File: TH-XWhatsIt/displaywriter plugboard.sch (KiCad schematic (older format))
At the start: 4 parts, among them J10 DISPLAYWRITER PLUGBOARD CONNE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, J11 DISPLAYWRITER PLUGBOARD ROWS, J9 DISPLAYWRITER PLUGBOARD COLUM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

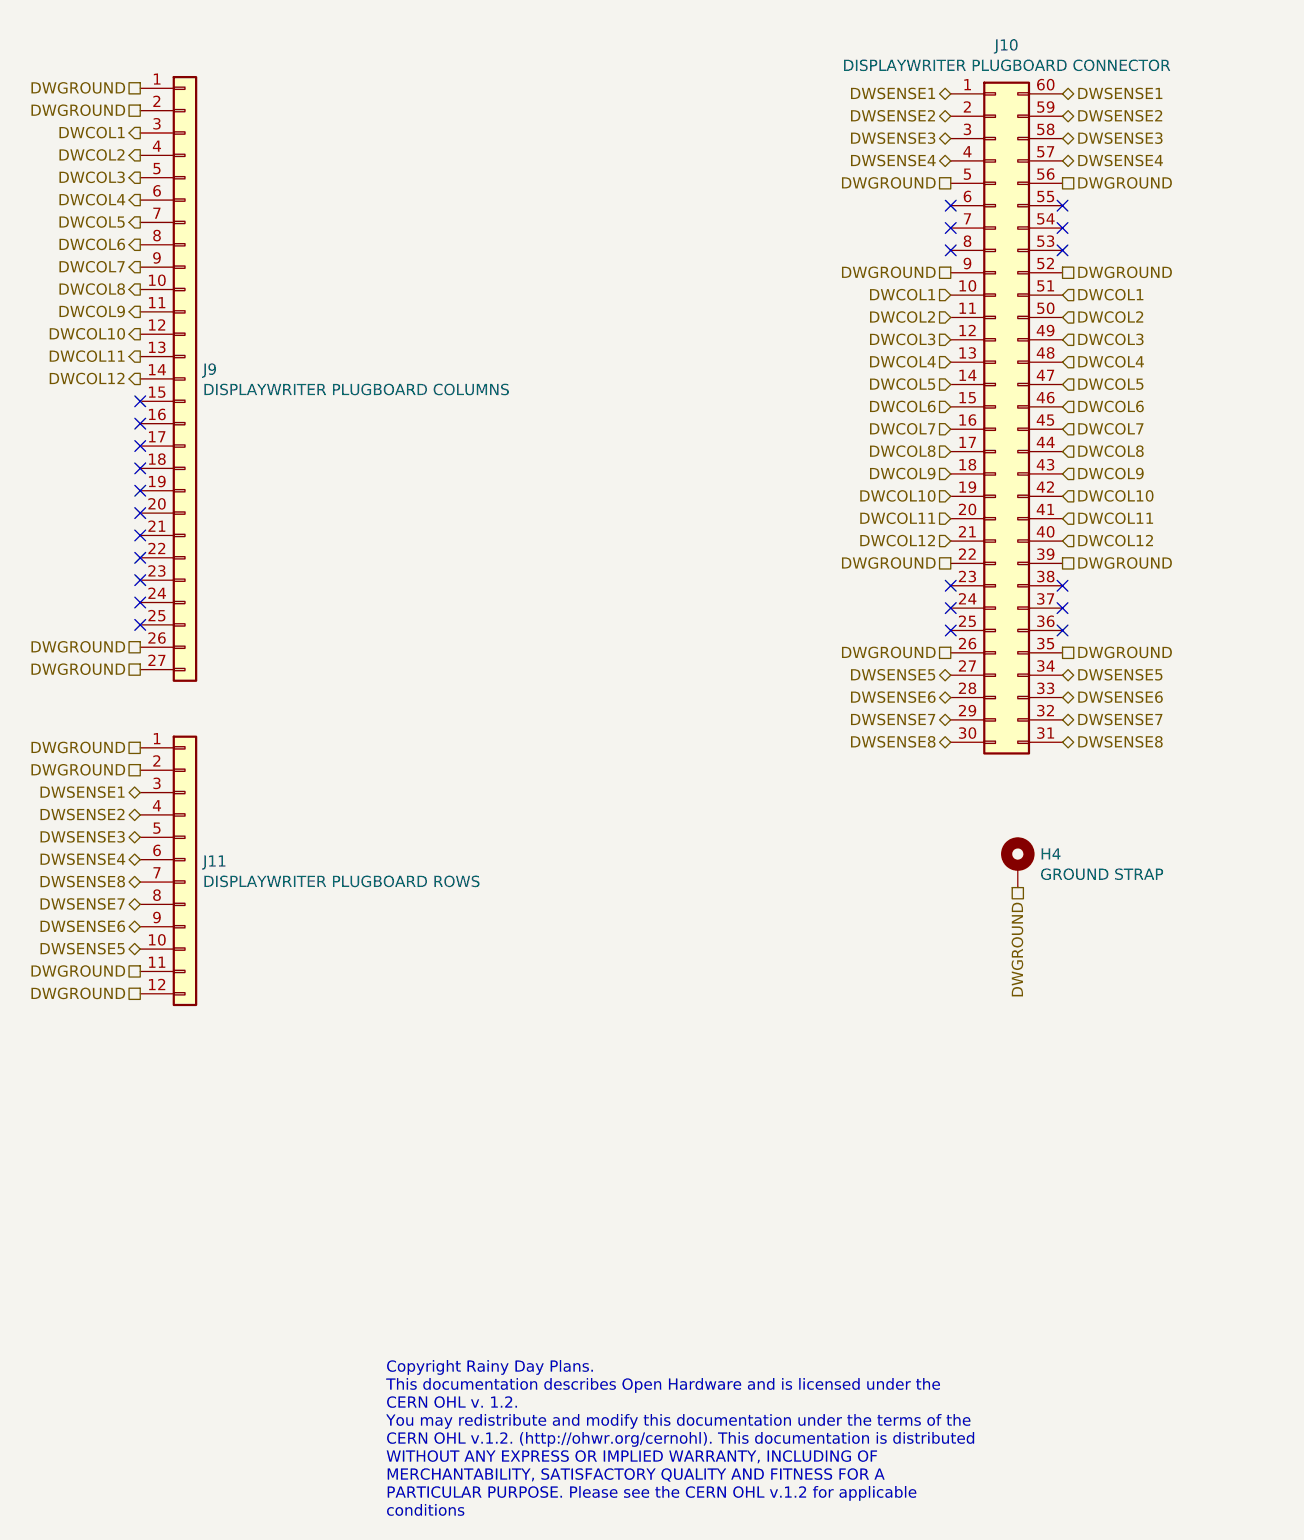
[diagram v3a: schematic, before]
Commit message: initial update to switch to smd, so now th prefix is a misnomer
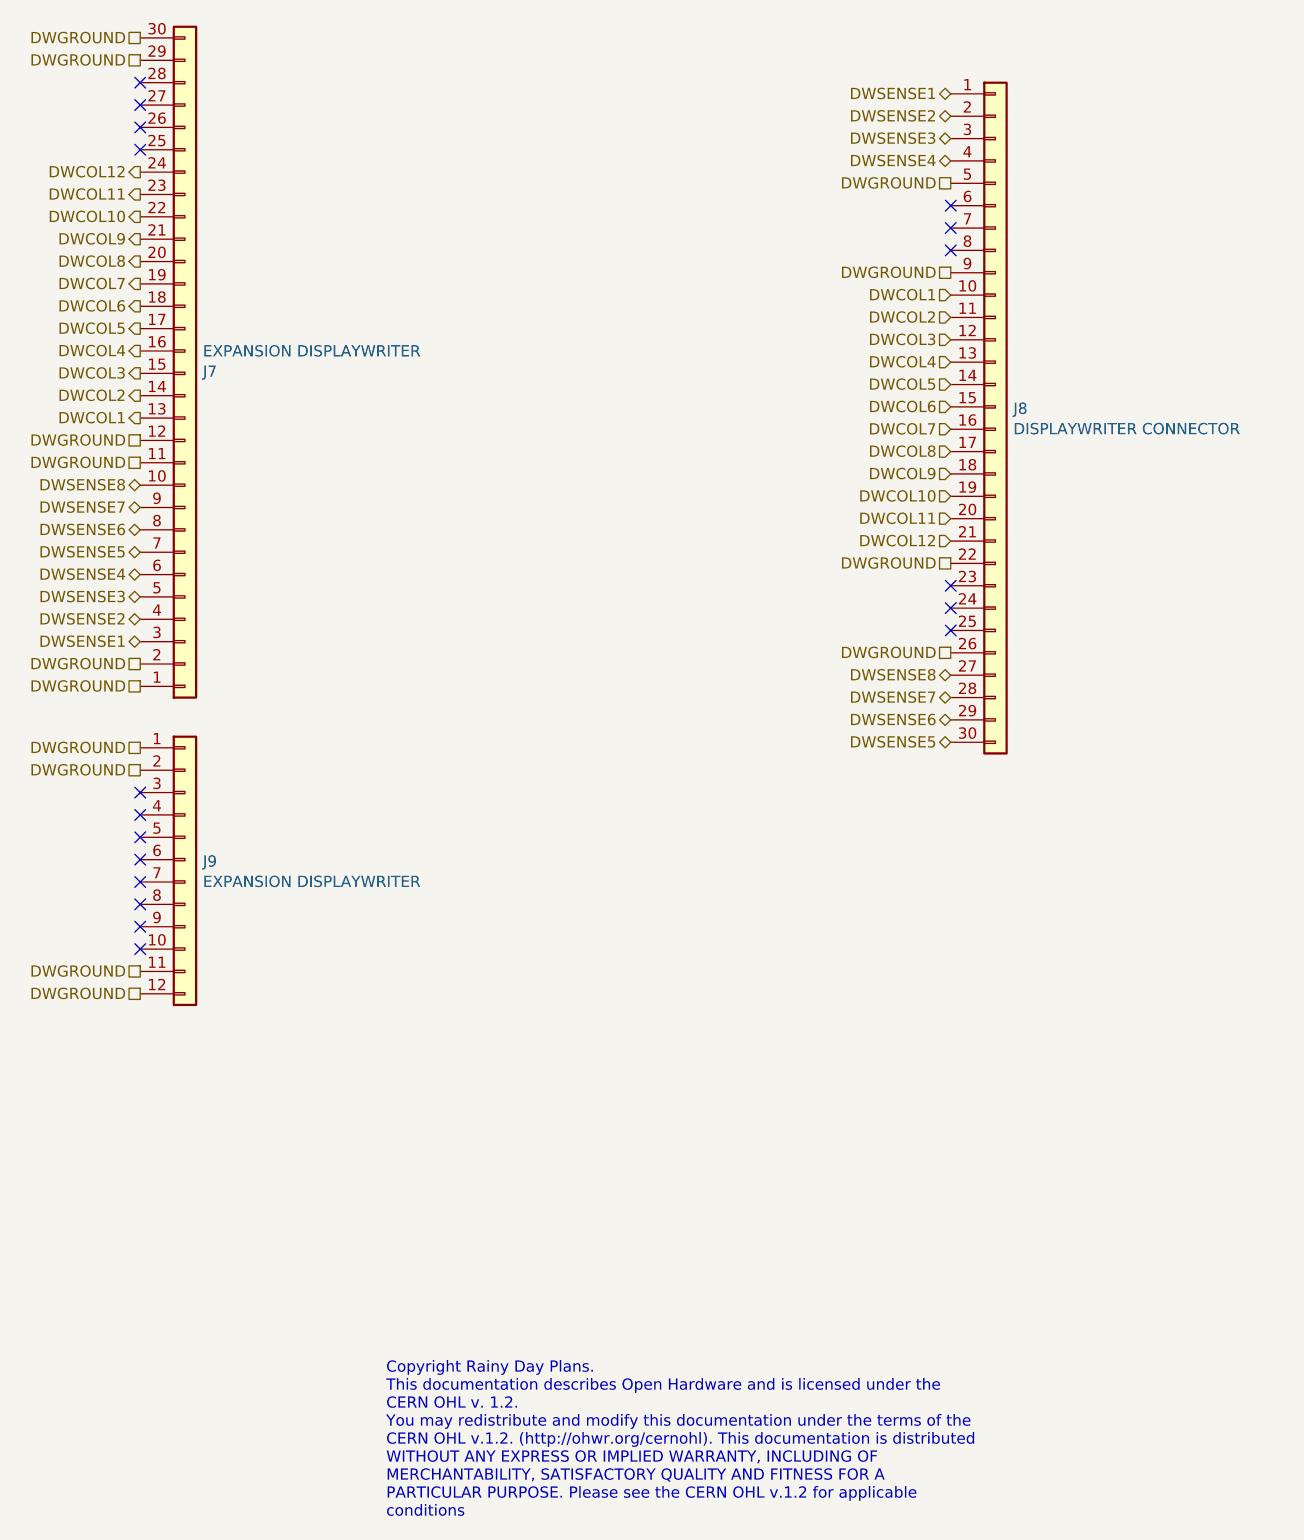
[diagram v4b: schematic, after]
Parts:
- removed H4: GROUND STRAP, MountingHole:MountingHole_2.2mm_M2_Pad_Via, symbol Mechanical:MountingHole_Pad
- removed J10: DISPLAYWRITER PLUGBOARD CONNECTOR, TH-XWhatsIt:DIP-60_155_ELL, symbol Connector_Generic:Conn_02x30_Counter_Clockwise
- removed J9: DISPLAYWRITER PLUGBOARD COLUMNS, Connector_PinSocket_2.54mm:PinSocket_1x27_P2.54mm_Vertical, symbol Connector_Generic:Conn_01x27
- added J7: EXPANSION DISPLAYWRITER, TH-XWhatsIt:30-pin-castelated-connector, symbol Connector_Generic:Conn_01x30
- added J8: DISPLAYWRITER CONNECTOR, TH-XWhatsIt:30-pin-universal-beamspring-connector, symbol Connector_Generic:Conn_01x30
- J9: renamed from J11; value DISPLAYWRITER PLUGBOARD ROWS -> EXPANSION DISPLAYWRITER; footprint Connector_PinSocket_2.54mm:PinSocket_1x12_P2.54mm_Vertical -> TH-XWhatsIt:12-pin-castelated-connector
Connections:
- net DWCOL1: now also J7.13 (Pin_13), J8.10 (Pin_10)
- net DWCOL10: now also J7.22 (Pin_22), J8.19 (Pin_19)
- net DWCOL11: now also J7.23 (Pin_23), J8.20 (Pin_20)
- net DWCOL12: now also J7.24 (Pin_24), J8.21 (Pin_21)
- net DWCOL2: now also J7.14 (Pin_14), J8.11 (Pin_11)
- net DWCOL3: now also J7.15 (Pin_15), J8.12 (Pin_12)
- net DWCOL4: now also J7.16 (Pin_16), J8.13 (Pin_13)
- net DWCOL5: now also J7.17 (Pin_17), J8.14 (Pin_14)
- net DWCOL6: now also J7.18 (Pin_18), J8.15 (Pin_15)
- net DWCOL7: now also J7.19 (Pin_19), J8.16 (Pin_16)
- net DWCOL8: now also J7.20 (Pin_20), J8.17 (Pin_17)
- net DWCOL9: now also J7.21 (Pin_21), J8.18 (Pin_18)
- net DWGROUND: now also J7.1 (Pin_1), J7.11 (Pin_11), J7.12 (Pin_12), J7.2 (Pin_2), J7.29 (Pin_29), J7.30 (Pin_30), J8.22 (Pin_22), J8.26 (Pin_26), J8.5 (Pin_5), J8.9 (Pin_9)
- net DWSENSE1: now also J7.3 (Pin_3), J8.1 (Pin_1); no longer J9.3 (Pin_3)
- net DWSENSE2: now also J7.4 (Pin_4), J8.2 (Pin_2); no longer J9.4 (Pin_4)
- net DWSENSE3: now also J7.5 (Pin_5), J8.3 (Pin_3); no longer J9.5 (Pin_5)
- net DWSENSE4: now also J7.6 (Pin_6), J8.4 (Pin_4); no longer J9.6 (Pin_6)
- net DWSENSE5: now also J7.7 (Pin_7), J8.30 (Pin_30); no longer J9.10 (Pin_10)
- net DWSENSE6: now also J7.8 (Pin_8), J8.29 (Pin_29); no longer J9.9 (Pin_9)
- net DWSENSE7: now also J7.9 (Pin_9), J8.28 (Pin_28); no longer J9.8 (Pin_8)
- net DWSENSE8: now also J7.10 (Pin_10), J8.27 (Pin_27); no longer J9.7 (Pin_7)
- no-connect marks 23 -> 18
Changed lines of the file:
@@
 $Descr A4 11693 8268
 encoding utf-8
-Sheet 4 4
+Sheet 3 3
 Title "Displaywriter plugboard to convert controller signals"
 Date "2020-01-31"
@@
 $EndDescr
 $Comp
-L Connector_Generic:Conn_01x27 J?
-U 1 1 5E97F100
-P 3050 2650
-AR Path="/5E97F100" Ref="J?"  Part="1"
-AR Path="/5E97697F/5E97F100" Ref="J?"  Part="1"
-AR Path="/5E995B14/5E97F100" Ref="J9"  Part="1"
-F 0 "J9" H 3130 2692 50  0000 L CNN
-F 1 "DISPLAYWRITER PLUGBOARD COLUMNS" H 3130 2601 50  0000 L CNN
-F 2 "Connector_PinSocket_2.54mm:PinSocket_1x27_P2.54mm_Vertical" H 3050 2650 50  0001 C CNN
-F 3 "~" H 3050 2650 50  0001 C CNN
-	1    3050 2650
-	1    0    0    -1
-$EndComp
-$Comp
 L Connector_Generic:Conn_01x12 J?
 U 1 1 5E97F11D
@@
 AR Path="/5E97F11D" Ref="J?"  Part="1"
 AR Path="/5E97697F/5E97F11D" Ref="J?"  Part="1"
-AR Path="/5E995B14/5E97F11D" Ref="J11"  Part="1"
-F 0 "J11" H 3130 4792 50  0000 L CNN
-F 1 "DISPLAYWRITER PLUGBOARD ROWS" H 3130 4701 50  0000 L CNN
-F 2 "Connector_PinSocket_2.54mm:PinSocket_1x12_P2.54mm_Vertical" H 3050 4800 50  0001 C CNN
+AR Path="/5E995B14/5E97F11D" Ref="J9"  Part="1"
+F 0 "J9" H 3130 4792 50  0000 L CNN
+F 1 "EXPANSION DISPLAYWRITER" H 3130 4701 50  0000 L CNN
+F 2 "TH-XWhatsIt:12-pin-castelated-connector" H 3050 4800 50  0001 C CNN
 F 3 "~" H 3050 4800 50  0001 C CNN
 	1    3050 4800
@@
 NoConn ~ 6475 1975
 NoConn ~ 6475 2075
-Text HLabel 2850 1550 0    50   Output ~ 0
-DWCOL1
-Text HLabel 2850 1650 0    50   Output ~ 0
-DWCOL2
-Text HLabel 2850 1750 0    50   Output ~ 0
-DWCOL3
-Text HLabel 2850 1850 0    50   Output ~ 0
-DWCOL4
-Text HLabel 2850 1950 0    50   Output ~ 0
-DWCOL5
-Text HLabel 2850 2050 0    50   Output ~ 0
-DWCOL6
-Text HLabel 2850 2150 0    50   Output ~ 0
-DWCOL7
-Text HLabel 2850 2250 0    50   Output ~ 0
-DWCOL8
-Text HLabel 2850 2350 0    50   Output ~ 0
-DWCOL9
-Text HLabel 2850 2450 0    50   Output ~ 0
-DWCOL10
-Text HLabel 2850 2550 0    50   Output ~ 0
-DWCOL11
-Text HLabel 2850 2650 0    50   Output ~ 0
-DWCOL12
-Text HLabel 2850 4500 0    50   BiDi ~ 0
-DWSENSE1
-Text HLabel 2850 4600 0    50   BiDi ~ 0
-DWSENSE2
-Text HLabel 2850 4700 0    50   BiDi ~ 0
-DWSENSE3
-Text HLabel 2850 4800 0    50   BiDi ~ 0
-DWSENSE4
-Text HLabel 2850 5200 0    50   BiDi ~ 0
-DWSENSE5
-Text HLabel 2850 5100 0    50   BiDi ~ 0
-DWSENSE6
-Text HLabel 2850 5000 0    50   BiDi ~ 0
-DWSENSE7
-Text HLabel 2850 4900 0    50   BiDi ~ 0
-DWSENSE8
 Text HLabel 6475 1375 0    50   BiDi ~ 0
 DWSENSE1
@@
 Text HLabel 6475 1675 0    50   BiDi ~ 0
 DWSENSE4
+Text HLabel 6475 4275 0    50   BiDi ~ 0
+DWSENSE5
+Text HLabel 6475 4175 0    50   BiDi ~ 0
+DWSENSE6
+Text HLabel 6475 4075 0    50   BiDi ~ 0
+DWSENSE7
 Text HLabel 6475 3975 0    50   BiDi ~ 0
-DWSENSE5
-Text HLabel 6475 4075 0    50   BiDi ~ 0
-DWSENSE6
-Text HLabel 6475 4175 0    50   BiDi ~ 0
-DWSENSE7
-Text HLabel 6475 4275 0    50   BiDi ~ 0
 DWSENSE8
 Text HLabel 6475 2275 0    50   Input ~ 0
@@
 Text HLabel 6475 3375 0    50   Input ~ 0
 DWCOL12
-Text HLabel 2850 1350 0    50   UnSpc ~ 0
+Text HLabel 2850 1125 0    50   UnSpc ~ 0
 DWGROUND
-Text HLabel 2850 1450 0    50   UnSpc ~ 0
+Text HLabel 2850 1225 0    50   UnSpc ~ 0
 DWGROUND
-Text HLabel 2850 3850 0    50   UnSpc ~ 0
+Text HLabel 2850 3925 0    50   UnSpc ~ 0
 DWGROUND
-Text HLabel 2850 3950 0    50   UnSpc ~ 0
+Text HLabel 2850 4025 0    50   UnSpc ~ 0
 DWGROUND
 Text HLabel 2850 4300 0    50   UnSpc ~ 0
@@
 Text HLabel 6475 3875 0    50   UnSpc ~ 0
 DWGROUND
-NoConn ~ 2850 2750
-NoConn ~ 2850 2850
-NoConn ~ 2850 2950
-NoConn ~ 2850 3050
-NoConn ~ 2850 3150
-NoConn ~ 2850 3250
-NoConn ~ 2850 3350
-NoConn ~ 2850 3450
-NoConn ~ 2850 3550
-NoConn ~ 2850 3650
-NoConn ~ 2850 3750
 Text Notes 3950 7750 0    50   ~ 0
 Copyright Rainy Day Plans.\nThis documentation describes Open Hardware and is licensed under the\nCERN OHL v. 1.2.\nYou may redistribute and modify this documentation under the terms of the\nCERN OHL v.1.2. (http://ohwr.org/cernohl). This documentation is distributed\nWITHOUT ANY EXPRESS OR IMPLIED WARRANTY, INCLUDING OF\nMERCHANTABILITY, SATISFACTORY QUALITY AND FITNESS FOR A\nPARTICULAR PURPOSE. Please see the CERN OHL v.1.2 for applicable\nconditions
+Text HLabel 2850 3825 0    50   BiDi ~ 0
+DWSENSE1
+Text HLabel 2850 3725 0    50   BiDi ~ 0
+DWSENSE2
+Text HLabel 2850 3625 0    50   BiDi ~ 0
+DWSENSE3
+Text HLabel 2850 3525 0    50   BiDi ~ 0
+DWSENSE4
+Text HLabel 2850 3425 0    50   BiDi ~ 0
+DWSENSE5
+Text HLabel 2850 3325 0    50   BiDi ~ 0
+DWSENSE6
+Text HLabel 2850 3225 0    50   BiDi ~ 0
+DWSENSE7
+Text HLabel 2850 3125 0    50   BiDi ~ 0
+DWSENSE8
+Text HLabel 2850 2925 0    50   UnSpc ~ 0
+DWGROUND
+Text HLabel 2850 3025 0    50   UnSpc ~ 0
+DWGROUND
 $Comp
-L Connector_Generic:Conn_02x30_Counter_Clockwise J10
-U 1 1 5E4284EA
+L Connector_Generic:Conn_01x30 J?
+U 1 1 5F5BFC0E
+P 3050 2625
+AR Path="/5F5BFC0E" Ref="J?"  Part="1"
+AR Path="/5E995B14/5F5BFC0E" Ref="J7"  Part="1"
+F 0 "J7" H 3130 2617 50  0000 L CNN
+F 1 "EXPANSION DISPLAYWRITER" H 3130 2526 50  0000 L CNN
+F 2 "TH-XWhatsIt:30-pin-castelated-connector" H 3050 2625 50  0001 C CNN
+F 3 "~" H 3050 2625 50  0001 C CNN
+	1    3050 2625
+	1    0    0    1
+$EndComp
+$Comp
+L Connector_Generic:Conn_01x30 J?
+U 1 1 5F5CA487
 P 6675 2775
-F 0 "J10" H 6725 4392 50  0000 C CNN
-F 1 "DISPLAYWRITER PLUGBOARD CONNECTOR" H 6725 4301 50  0000 C CNN
-F 2 "TH-XWhatsIt:DIP-60_155_ELL" H 6675 2775 50  0001 C CNN
+AR Path="/5F5CA487" Ref="J?"  Part="1"
+AR Path="/5E995B14/5F5CA487" Ref="J8"  Part="1"
+F 0 "J8" H 6755 2767 50  0000 L CNN
+F 1 "DISPLAYWRITER CONNECTOR" H 6755 2676 50  0000 L CNN
+F 2 "TH-XWhatsIt:30-pin-universal-beamspring-connector" H 6675 2775 50  0001 C CNN
 F 3 "~" H 6675 2775 50  0001 C CNN
 	1    6675 2775
 	1    0    0    -1
 $EndComp
-NoConn ~ 6975 3575
-NoConn ~ 6975 3675
-NoConn ~ 6975 3775
-NoConn ~ 6975 1875
-NoConn ~ 6975 1975
-NoConn ~ 6975 2075
-Text HLabel 6975 1375 2    50   BiDi ~ 0
-DWSENSE1
-Text HLabel 6975 1475 2    50   BiDi ~ 0
-DWSENSE2
-Text HLabel 6975 1575 2    50   BiDi ~ 0
-DWSENSE3
-Text HLabel 6975 1675 2    50   BiDi ~ 0
-DWSENSE4
-Text HLabel 6975 3975 2    50   BiDi ~ 0
-DWSENSE5
-Text HLabel 6975 4075 2    50   BiDi ~ 0
-DWSENSE6
-Text HLabel 6975 4175 2    50   BiDi ~ 0
-DWSENSE7
-Text HLabel 6975 4275 2    50   BiDi ~ 0
-DWSENSE8
-Text HLabel 6975 2275 2    50   Input ~ 0
+NoConn ~ 2850 4500
+NoConn ~ 2850 4600
+NoConn ~ 2850 4700
+NoConn ~ 2850 4800
+NoConn ~ 2850 4900
+NoConn ~ 2850 5000
+NoConn ~ 2850 5100
+NoConn ~ 2850 5200
+Text HLabel 2850 1725 0    50   Output ~ 0
+DWCOL12
+Text HLabel 2850 1825 0    50   Output ~ 0
+DWCOL11
+Text HLabel 2850 1925 0    50   Output ~ 0
+DWCOL10
+Text HLabel 2850 2025 0    50   Output ~ 0
+DWCOL9
+Text HLabel 2850 2125 0    50   Output ~ 0
+DWCOL8
+Text HLabel 2850 2225 0    50   Output ~ 0
+DWCOL7
+Text HLabel 2850 2325 0    50   Output ~ 0
+DWCOL6
+Text HLabel 2850 2425 0    50   Output ~ 0
+DWCOL5
+Text HLabel 2850 2525 0    50   Output ~ 0
+DWCOL4
+Text HLabel 2850 2625 0    50   Output ~ 0
+DWCOL3
+Text HLabel 2850 2725 0    50   Output ~ 0
+DWCOL2
+Text HLabel 2850 2825 0    50   Output ~ 0
 DWCOL1
-Text HLabel 6975 2375 2    50   Input ~ 0
-DWCOL2
-Text HLabel 6975 2475 2    50   Input ~ 0
-DWCOL3
-Text HLabel 6975 2575 2    50   Input ~ 0
-DWCOL4
-Text HLabel 6975 2675 2    50   Input ~ 0
-DWCOL5
-Text HLabel 6975 2775 2    50   Input ~ 0
-DWCOL6
-Text HLabel 6975 2875 2    50   Input ~ 0
-DWCOL7
-Text HLabel 6975 2975 2    50   Input ~ 0
-DWCOL8
-Text HLabel 6975 3075 2    50   Input ~ 0
-DWCOL9
-Text HLabel 6975 3175 2    50   Input ~ 0
-DWCOL10
-Text HLabel 6975 3275 2    50   Input ~ 0
-DWCOL11
-Text HLabel 6975 3375 2    50   Input ~ 0
-DWCOL12
-Text HLabel 6975 1775 2    50   UnSpc ~ 0
-DWGROUND
-Text HLabel 6975 2175 2    50   UnSpc ~ 0
-DWGROUND
-Text HLabel 6975 3475 2    50   UnSpc ~ 0
-DWGROUND
-Text HLabel 6975 3875 2    50   UnSpc ~ 0
-DWGROUND
-$Comp
-L Mechanical:MountingHole_Pad H4
-U 1 1 5E3A0C5C
-P 6775 4825
-F 0 "H4" H 6875 4874 50  0000 L CNN
-F 1 "GROUND STRAP" H 6875 4783 50  0000 L CNN
-F 2 "MountingHole:MountingHole_2.2mm_M2_Pad_Via" H 6775 4825 50  0001 C CNN
-F 3 "~" H 6775 4825 50  0001 C CNN
-	1    6775 4825
-	1    0    0    -1
-$EndComp
-Text HLabel 6775 4925 3    50   UnSpc ~ 0
-DWGROUND
+NoConn ~ 2850 1325
+NoConn ~ 2850 1425
+NoConn ~ 2850 1525
+NoConn ~ 2850 1625
 $EndSCHEMATC

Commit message: Using new footprint for displaywriter too
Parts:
- J8: footprint TH-XWhatsIt:30-pin-universal-beamspring-connector -> TH-XWhatsIt:30-pin-universal-displaywriter-connector_v2
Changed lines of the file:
@@
 F 0 "J8" H 6755 2767 50  0000 L CNN
 F 1 "DISPLAYWRITER CONNECTOR" H 6755 2676 50  0000 L CNN
-F 2 "TH-XWhatsIt:30-pin-universal-beamspring-connector" H 6675 2775 50  0001 C CNN
+F 2 "TH-XWhatsIt:30-pin-universal-displaywriter-connector_v2" H 6675 2775 50  0001 C CNN
 F 3 "~" H 6675 2775 50  0001 C CNN
 	1    6675 2775
